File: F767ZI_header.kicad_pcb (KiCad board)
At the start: 2 copper layers, 82.6 x 99.1 mm, 25 parts, among them J1 I2C2_MD, J2 CAN1, J3 CAN2, J4 UART, J5 PowerBoard, J6 EMERSW_CON, J7 I2C1_default, J9 RESET_SW, SW1 SW_Push, U1 MCP2562-E-P, U2 MCP2562-E-P

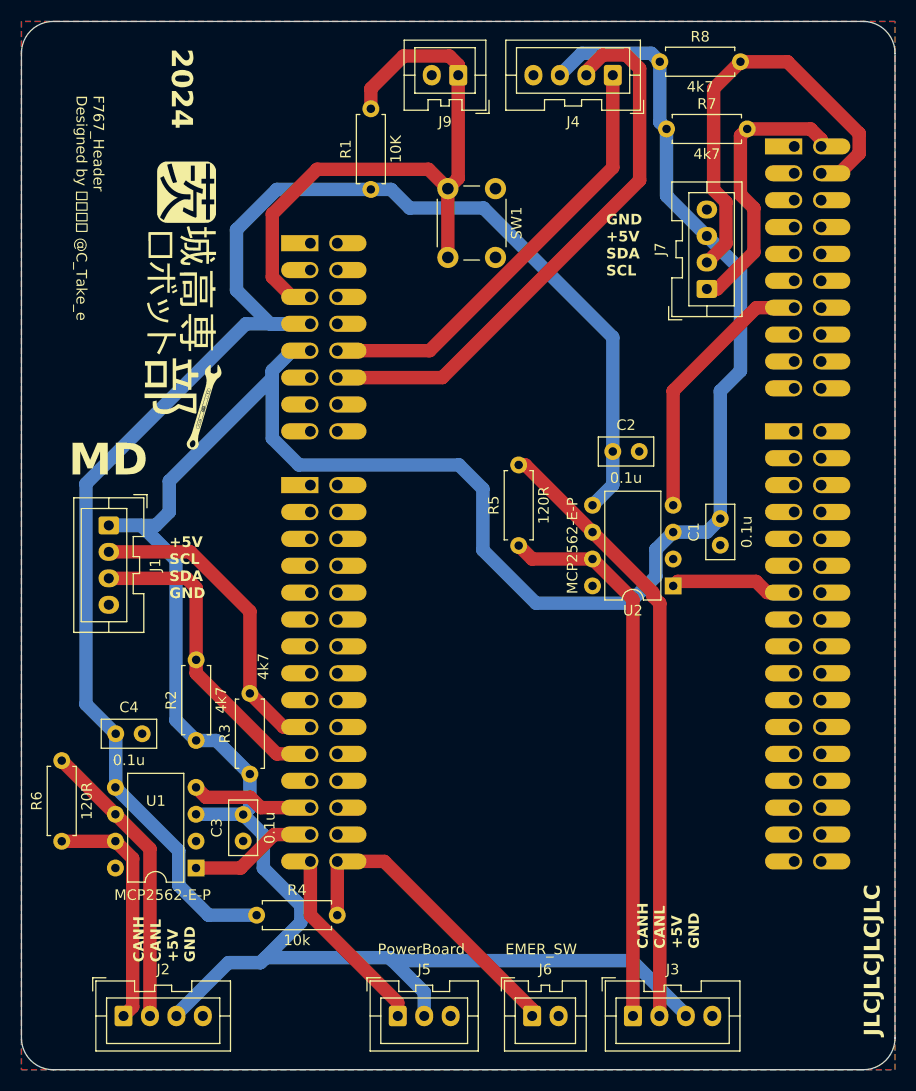
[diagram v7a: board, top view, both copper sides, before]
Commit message: PCB: 外形調整
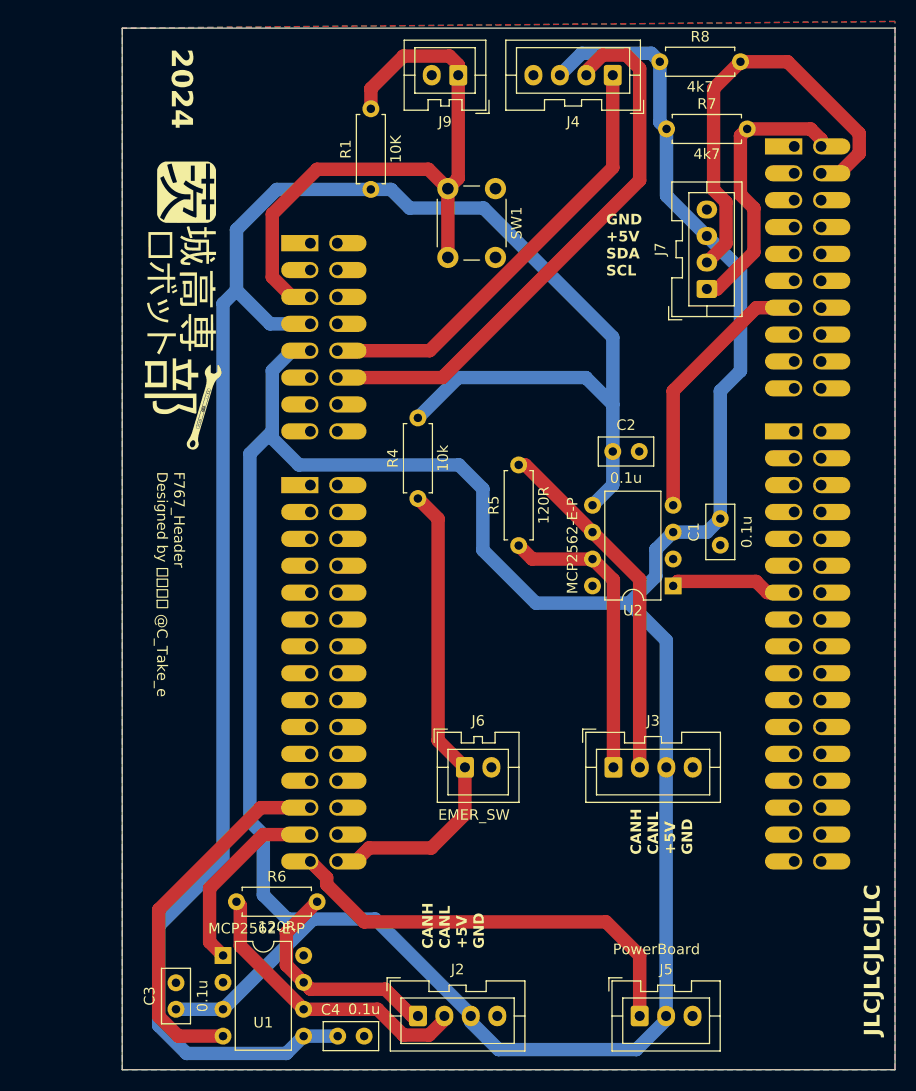
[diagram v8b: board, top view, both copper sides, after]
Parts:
- removed J1: I2C2_MD, Connector_JST:JST_XA_B04B-XASK-1_1x04_P2.50mm_Vertical
- removed R2, R3: 4k7, Resistor_THT:R_Axial_DIN0207_L6.3mm_D2.5mm_P7.62mm_Horizontal
- moved R4 49.4 mm to (182.2, 87.0), turned to -90 degrees
- moved C4 35.4 mm to (174.7, 145.4)
- moved J2 27.8 mm to (182.2, 143.5)
- moved R6 24.8 mm to (172.7, 132.7), turned to 180 degrees
- moved J6 24.3 mm to (186.7, 120.0)
- moved J3 23.6 mm to (200.7, 120.0)
- moved J5 22.9 mm to (203.2, 143.5)
- moved C3 19.5 mm to (159.4, 142.9), turned to 90 degrees
- moved U1 8.65 mm to (163.8, 137.8), turned to 0 degrees
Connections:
- A1 pad CN9_19: I2C2_SCL -> unconnected-(A1C-D69/PF_1/I2C_B_SCL-PadCN9_19)
- A1 pad CN9_21: I2C2_SDA -> unconnected-(A1C-D68/PF_0/I2C_B_SDA-PadCN9_21)
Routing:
- net +3V3: track 151.3 -> 185.9 mm
- net I2C2_SDA: track 30.6 -> 0.00 mm
- net I2C2_SCL: track 30.4 -> 0.00 mm
- net CAN2L: track 58.0 -> 33.7 mm
- net CAN2H: track 52.3 -> 28.0 mm
- net CAN1_RD: track 11.6 -> 35.3 mm
- net EMER_SIG: track 18.0 -> 40.9 mm
- net EMER_SW: track 29.9 -> 45.6 mm
- net +5V: track 269.0 -> 275.5 mm
- net CAN1_TD: track 12.1 -> 18.5 mm
- net CAN1H: track 22.6 -> 21.6 mm
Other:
- board size 82.6 x 99.1 mm -> 73 x 98.4 mm
- board text removed: "+5V SCL SDA GND"
- board text removed: "MD"
